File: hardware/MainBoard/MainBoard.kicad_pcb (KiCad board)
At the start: 4 copper layers, 28 x 58.4 mm, 55 parts, among them J1 Conn_02x16_Top_Bottom, J2 Conn_02x16_Top_Bottom, J3 USB_C_Receptacle_USB2.0_16P, J4 En_A, J5 En_B, J6 Micro_SD_Card_Det2, J7 Conn_02x16_Top_Bottom, Q2 FDN340P, Q3 FDN340P, U1 ESP32-S3-WROOM-1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

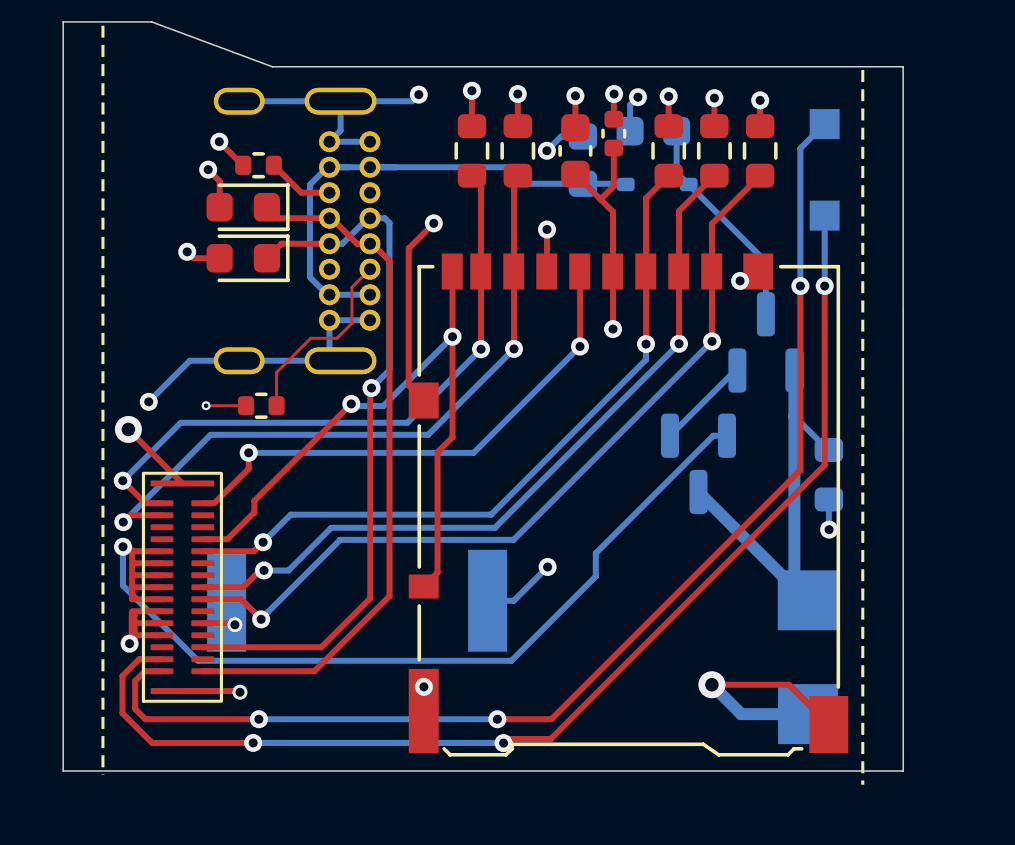
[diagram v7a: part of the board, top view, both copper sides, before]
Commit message: changed voltage selector to actually work
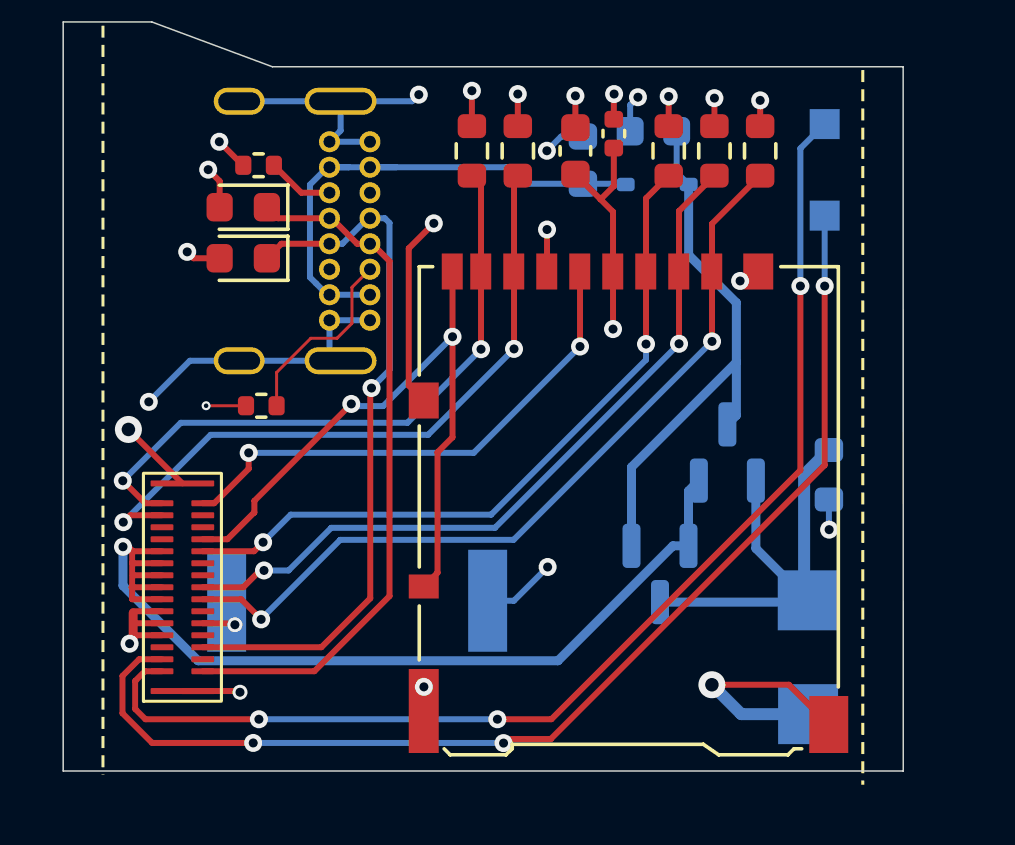
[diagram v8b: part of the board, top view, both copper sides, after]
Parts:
- moved Q2 8.49 mm to (82.4, 103.2), turned to -90 degrees
- moved Q3 1.03 mm to (84.7, 99.1), turned to 90 degrees
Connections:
- Q2 pad 1: LIPO PWR -> VBUS
- Q2 pad 2: PWR_SELECT -> CONN_21
- Q2 pad 3: VBUS -> LIPO PWR
- Q3 pad 1: PWR_SELECT -> LIPO PWR
- Q3 pad 3: LIPO PWR -> VBUS
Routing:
- net VBUS: track 7.33 -> 18.3 mm
- net PWR_SELECT: track 3.15 -> 0.00 mm
- net LIPO PWR: track 14.6 -> 15.7 mm
- net CONN_21: track 82.9 -> 81.9 mm
